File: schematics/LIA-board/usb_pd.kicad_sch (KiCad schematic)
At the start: 1 part, among them U21 STUSB4500QTR

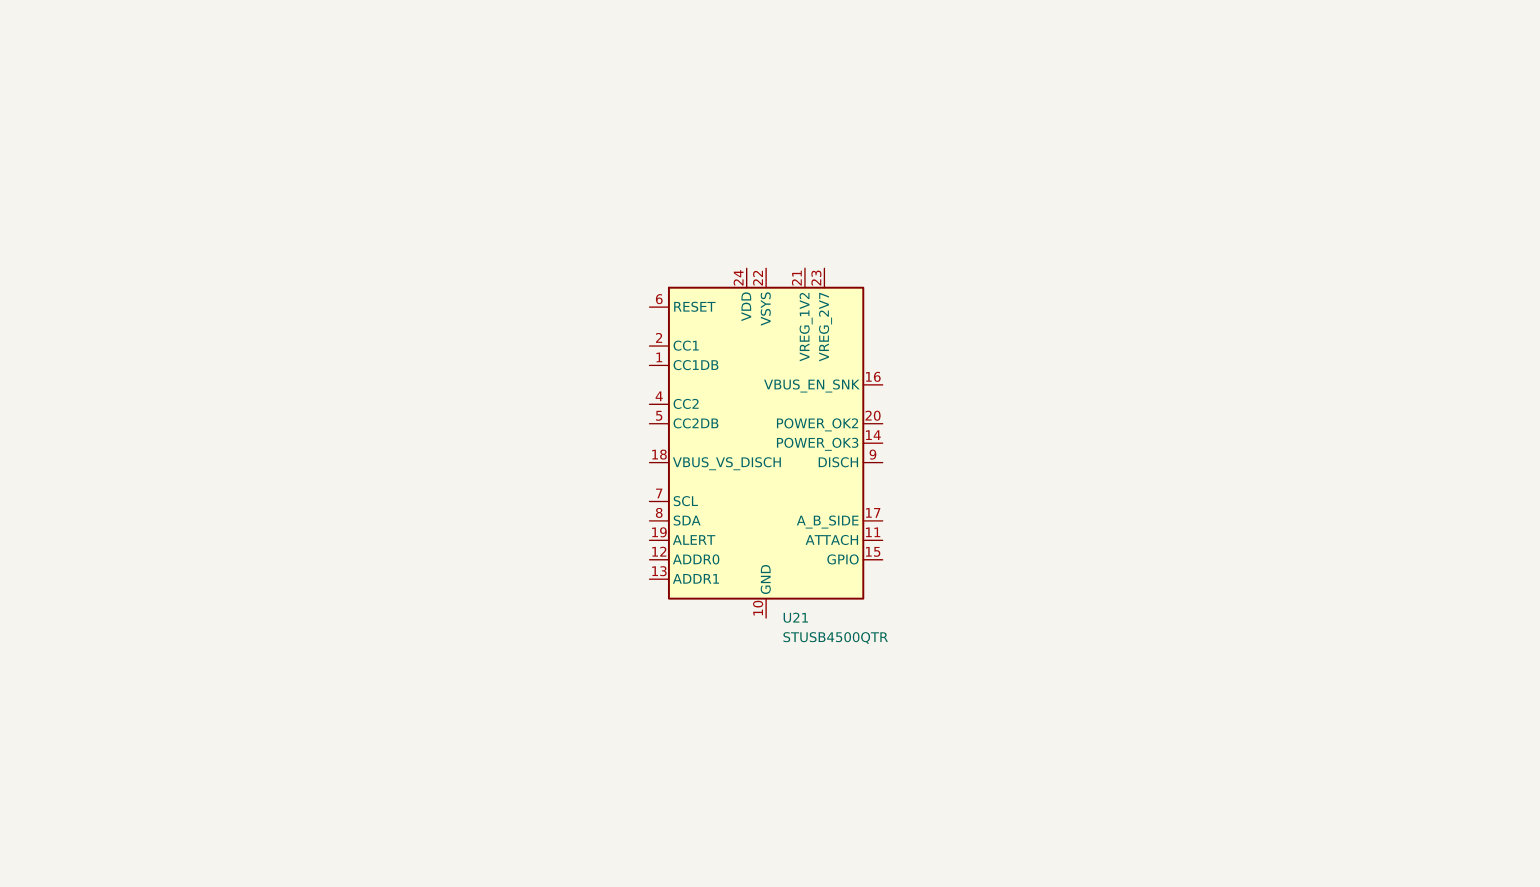
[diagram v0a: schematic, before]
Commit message: commit before changing the oscillator implementation
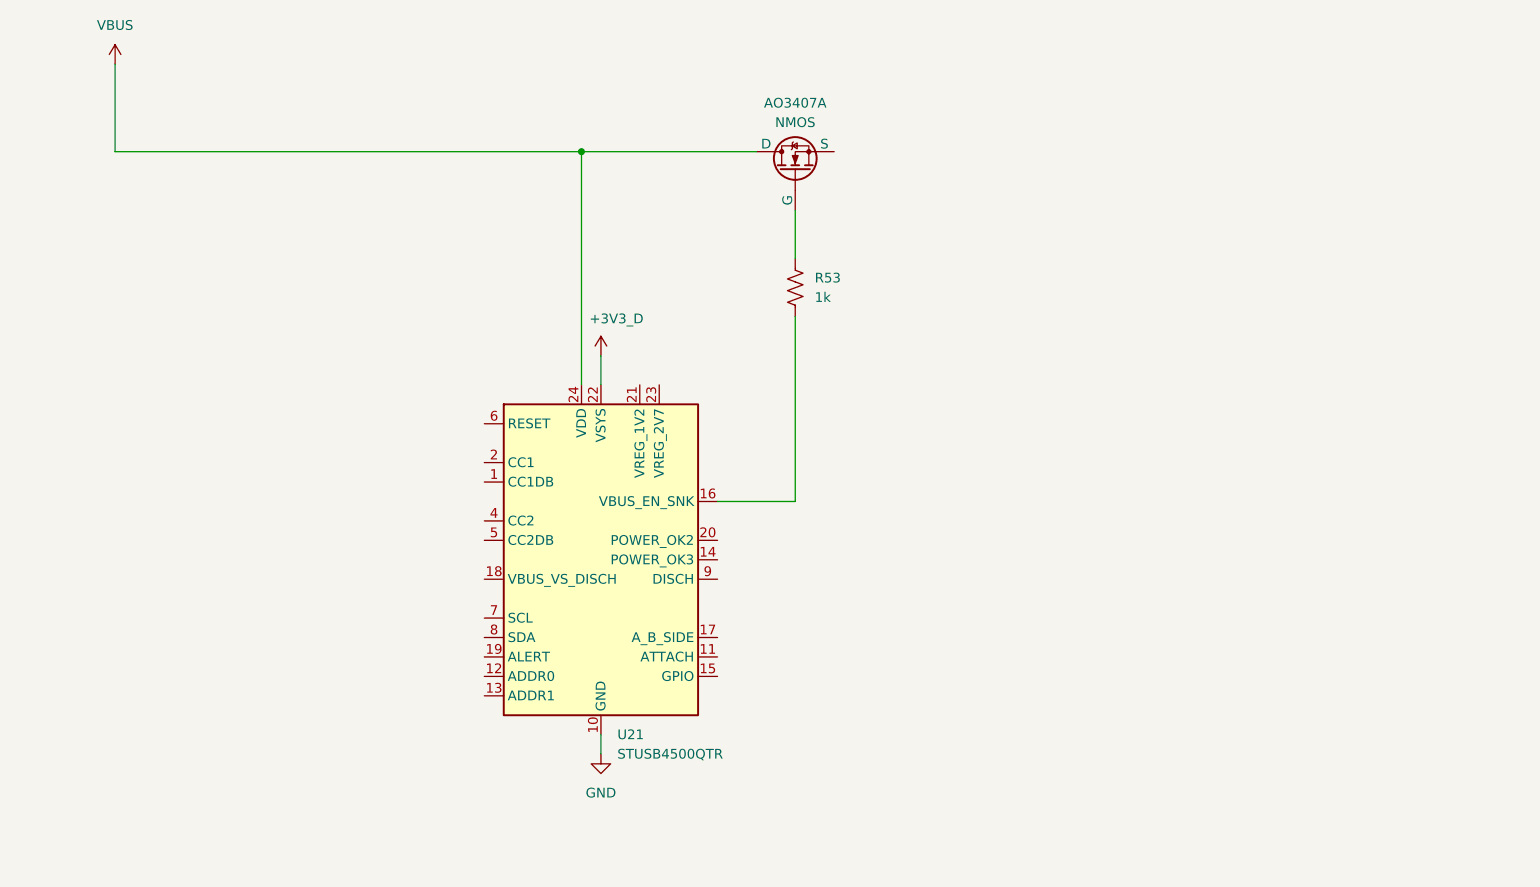
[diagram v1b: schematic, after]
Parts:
- added AO3407A: NMOS, symbol Simulation_SPICE:NMOS
- added R53: 1k, SparkFun-Resistor:R_0603_1608Metric, symbol SparkFun:R
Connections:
- net GND: now reaches U21.10 (GND), U21.25 (GND)
- net at U21.16 (VBUS_EN_SNK): now also R53.2
- net +3V3_D: now reaches U21.22 (VSYS)
- net VBUS: now reaches U21.24 (VDD)
- net VBUS: now also AO3407A.1 (D)
- new net: AO3407A.2 (G), R53.1
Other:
- moved on the sheet: U21

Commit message: commit before changing LIA
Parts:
- removed AO3407A: NMOS, symbol Simulation_SPICE:NMOS
- added C46, C47, C48: 1uF, symbol Device:C
- added Q1: AO3407A, symbol Transistor_FET:Q_PMOS_GSD
- added R42: 100k, SparkFun-Resistor:R_0603_1608Metric, symbol SparkFun:R
- added R44, R45, R46, R47: 1k, SparkFun-Resistor:R_0603_1608Metric, symbol SparkFun:R
- added R48, R49, R50, R51: 4.7k, SparkFun-Resistor:R_0603_1608Metric, symbol SparkFun:R
- renumbered R53 to R32, U21 to U13
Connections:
- net +3V3_D: now also R48.1, R49.1, R50.1, R51.1
- net GND: now also U13.12 (ADDR0), U13.13 (ADDR1), C46.2, C47.2, C48.2, R47.2
- net at R32.1: now also Q1.1 (G)
- net at R32.2, U13.16 (VBUS_EN_SNK): now also R42.2
- net usb_cc1: now reaches U13.1 (CC1DB)
- net usb_cc1: now also U13.2 (CC1)
- net usb_pd_attach: now reaches U13.11 (ATTACH)
- net usb_pd_attach: now also R51.2
- net at U13.18 (VBUS_VS_DISCH): now also R45.2
- net usb_pd_alert: now reaches U13.19 (ALERT)
- net usb_pd_alert: now also R50.2
- net at U13.21 (VREG_1V2): now also C46.1
- net at U13.23 (VREG_2V7): now also C47.1
- net usb_cc2: now reaches U13.4 (CC2)
- net usb_cc2: now also U13.5 (CC2DB)
- net usb_dp_rst: now reaches U13.6 (RESET)
- net usb_dp_rst: now also R47.1
- net i2c_scl: now reaches U13.7 (SCL)
- net i2c_scl: now also R48.2
- net i2c_sda: now reaches U13.8 (SDA)
- net i2c_sda: now also R49.2
- net at U13.9 (DISCH): now also R46.2
- net VBUS renamed VBUS_PD
- net VBUS_PD: now also C48.1, Q1.2 (S), R42.1, R44.1
- new net: R44.2, R45.1
- new net V_USB_PD: Q1.3 (D), R46.1
- no-connect marks 0 -> 4
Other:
- moved on the sheet: R32, U13
